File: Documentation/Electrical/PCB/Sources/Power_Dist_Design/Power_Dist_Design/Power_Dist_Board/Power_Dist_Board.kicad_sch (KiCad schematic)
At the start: 47 parts, among them J1 Battery Connector, J2 5V Connector, J3 3.3V Connector, M1 Motor_DC, M2 Motor_DC, M3 Motor_DC, M4 Motor_DC, M5 Motor_DC, M6 Motor_DC, SW1 Emergency Stop, U1 TPS565201, U2 TPS565201

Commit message: Made further edits to pcb
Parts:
- removed J2: 5V Connector, Connector_Phoenix_MSTB:PhoenixContact_MSTBVA_2,5_2-G-5,08_1x02_P5.08mm_Vertical, symbol Connector:Conn_01x02_Female
- removed J3: 3.3V Connector, Connector_Phoenix_MSTB:PhoenixContact_MSTBVA_2,5_2-G-5,08_1x02_P5.08mm_Vertical, symbol Connector:Conn_01x02_Female
- added J2, J3: 5V_Power_Rail, Power_Dist:Pwr_Rail_Conn_Custom, symbol Connector:Conn_01x01_Female
- added J4, J5: 3.3V_Power_Rail, Power_Dist:Pwr_Rail_Conn_Custom, symbol Connector:Conn_01x01_Female
- added J6, J7: GND_Rail, Power_Dist:Pwr_Rail_Conn_Custom, symbol Connector:Conn_01x01_Female
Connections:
- net +3.3V: now also J4.1 (Pin_1), J5.1 (Pin_1)
- net +5V: now also J2.1 (Pin_1), J3.1 (Pin_1)
- net GND: now also J6.1 (Pin_1), J7.1 (Pin_1)
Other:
- note removed: "nts: make vout and sw traces wider for high current for power rails make periodic holes that can be used for screw terminals, female headers, etc."

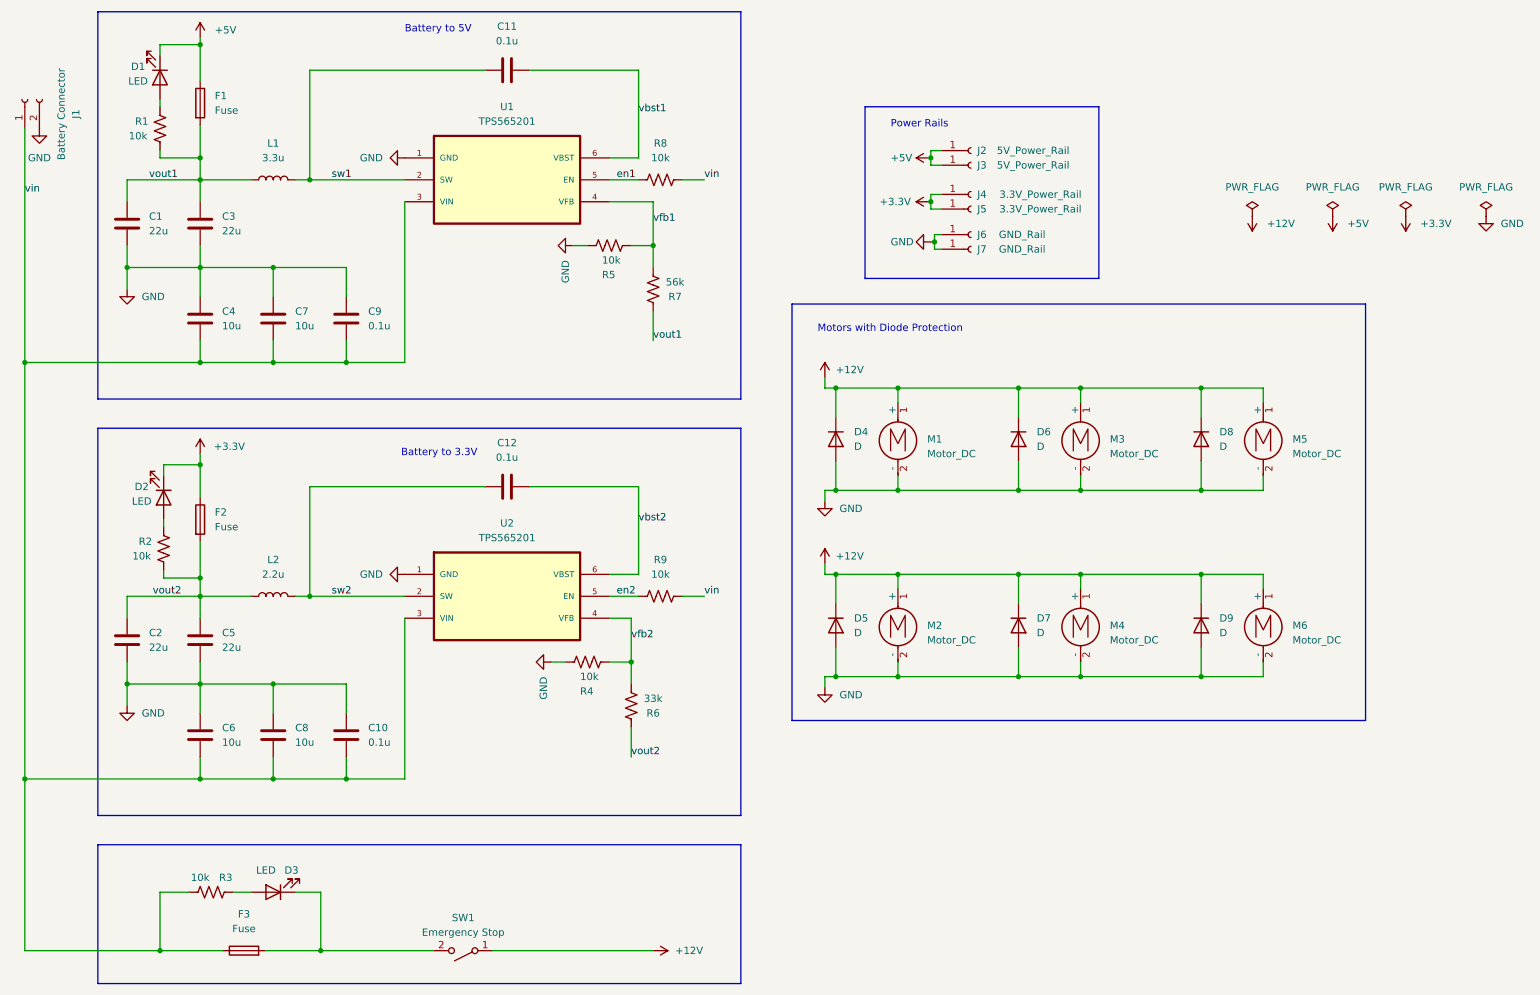
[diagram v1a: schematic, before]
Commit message: Added more motor terminals
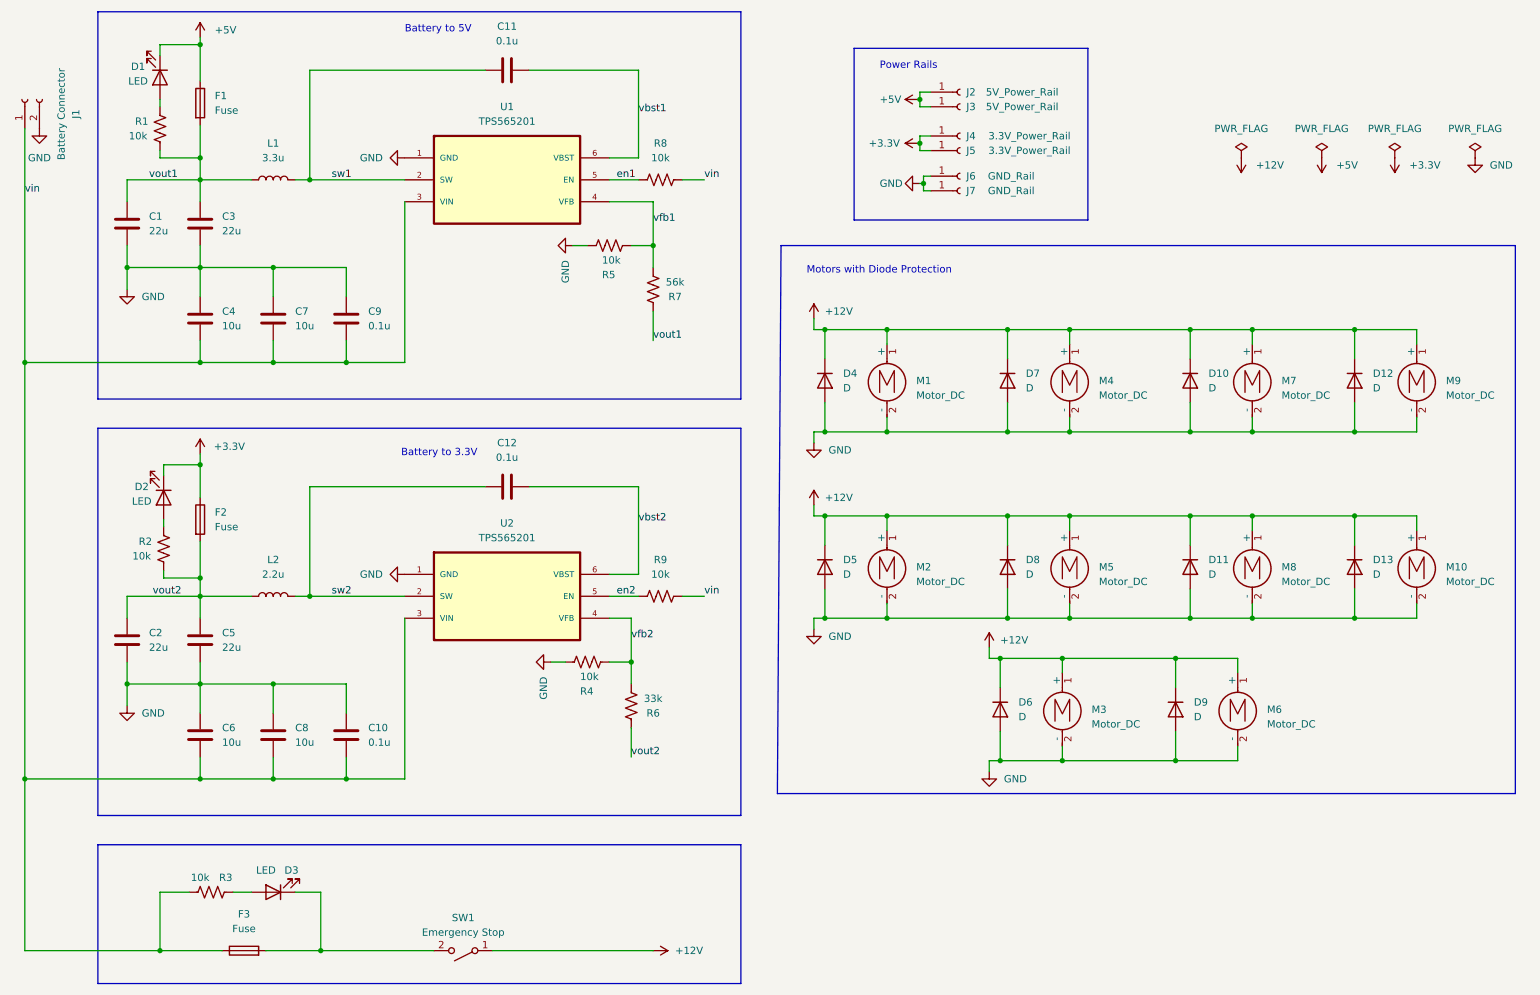
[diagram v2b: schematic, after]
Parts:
- added D12, D13, D6, D9: D, RB070MM:DIO_RB051MM_ROM-M, symbol Device:D
- added M10, M3, M6, M9: Motor_DC, Power_Dist:Molex_Screw_Term_0397730002, symbol Motor:Motor_DC
- renumbered D8 to D10, D9 to D11, D6 to D7, D7 to D8, M3 to M4, M4 to M5, M5 to M7, M6 to M8
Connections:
- net +12V: now also D12.1 (K), D13.1 (K), D6.1 (K), D9.1 (K), M10.1 (+), M3.1 (+), M6.1 (+), M9.1 (+)
- net GND: now also D12.2 (A), D13.2 (A), D6.2 (A), D9.2 (A), M10.2 (-), M3.2 (-), M6.2 (-), M9.2 (-)
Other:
- moved on the sheet: D10, D11, D4, D5, D7, D8, J2, J3, J4, J5, J6, J7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
